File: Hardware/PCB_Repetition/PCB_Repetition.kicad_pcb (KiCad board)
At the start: 2 copper layers, 519.9 x 88.9 mm, 100 parts, among them J1 Conn_01x03, J10 XLR3, J11 XLR3, J12 XLR3, J13 XLR3, J14 XLR3, J15 XLR3, J16 XLR3, J17 XLR3, J18 XLR3, J2 XLR3, J3 XLR3, J4 Conn_01x03, J5 Conn_01x03, J6 Conn_01x03, J7 XLR3, J8 XLR3, J9 XLR3, Q1 SQ2310ES-T1_BE3, Q2 SQ2310ES-T1_BE3, Q3 SQ2310ES-T1_BE3, Q4 SQ2310ES-T1_BE3, Q5 SQ2310ES-T1_BE3, Q6 SQ2310ES-T1_BE3, SW1 SW_SPST, SW2 SW_SPST, SW3 SW_DIP_x02, SW4 SW_DIP_x02, SW5 SW_DIP_x02, SW6 SW_DIP_x02, SW7 SW_DIP_x02, SW8 SW_DIP_x02, U2 ZXBM5210-SP, U4 PCF8575DBR

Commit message: Final change
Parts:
- added G***: LOGO, img:Dessin_CoventGarden, B.Cu at (508.1, 203.5)
- added G***: LOGO, img:Logo_Covent, B.Cu at (508.0, 189.3)
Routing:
- net /INA3_2: track 76.8 -> 77.5 mm
- net GND: vias 878 -> 889
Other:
- board text added: "By Capodagli Janus"

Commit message: finalisation v2 PCB repetition
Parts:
- removed C13, C14, C15, C16, C18: 100n, Capacitor_SMD:C_0603_1608Metric_Pad1.08x0.95mm_HandSolder
- removed D10, D11, D12, D6, D8: WS2812B, LED_SMD:LED_WS2812B_PLCC4_5.0x5.0mm_P3.2mm
- added SW9: SW_DIP_x02, DIP_Switch:DIP_SW_1x02_P2.54mm, F.Cu at (204.7, 185.4)
- C17, C4, C5, Q1, Q2, Q3, Q4, Q5, Q6, R10, R11, R12, R13, R14, R15, R16, R17, R18, R7, R8, R9, U2, U4: moved to F.Cu
- J10, J11, J12, J13, J14, J15, J16, J17, J18, J2, J3, J7, J8, J9: moved to B.Cu
- U1: footprint ESP32_SuperMini:SuperMini SMT -> ESP32_SuperMini:C3_SuperMini
- moved G*** 426.1 mm to (83.7, 165.5)
- moved G*** 424.7 mm to (83.5, 176.9)
- moved J18 270.4 mm to (251.4, 216.0), turned to 180 degrees
- moved C12 250.6 mm to (73.4, 193.8), turned to 90 degrees
- moved J16 200.8 mm to (281.4, 216.0), turned to 180 degrees
- moved J12 186.5 mm to (341.4, 216.0), turned to 180 degrees
- moved U13 179.4 mm to (229.0, 187.0), turned to 0 degrees
- moved SW8 161.5 mm to (246.0, 189.0), turned to -90 degrees
- moved J17 145.5 mm to (244.0, 168.0), turned to 180 degrees
- moved J14 131.6 mm to (311.4, 216.0), turned to 180 degrees
- moved H7 130.0 mm to (417.6, 231.3)
- moved H5 130.0 mm to (417.6, 154.5)
- moved J10 122.4 mm to (371.4, 216.0), turned to 180 degrees
- moved J7 117.5 mm to (394.0, 168.0), turned to 180 degrees
- moved SW3 99.9 mm to (396.0, 189.0), turned to -90 degrees
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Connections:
- net /Relais_XLR1/GND2 renamed /Relais_XLR1/GND_entree
- net /Relais_XLR2/GND2 renamed /Relais_XLR2/GND_entree
- net /Relais_XLR3/GND2 renamed /Relais_XLR3/GND_entree
- net /Relais_XLR4/GND2 renamed /Relais_XLR4/GND_entree
- net /Relais_XLR5/GND2 renamed /Relais_XLR5/GND_entree
- net /Relais_XLR6/GND2 renamed /Relais_XLR6/GND_entree
- D5 pad 2: Net-(D5-DOUT) -> unconnected-(D5-DOUT-Pad2)
- H2 pad 1: unconnected-(H2-Pad1)_2 -> Earth
- H3 pad 1: Earth -> GND
- J10 pad 1: GND -> /Relais_XLR2/GND_sortie
- J12 pad 1: GND -> /Relais_XLR3/GND_sortie
- J14 pad 1: GND -> /Relais_XLR4/GND_sortie
- J16 pad 1: GND -> /Relais_XLR5/GND_sortie
- J18 pad 1: GND -> /Relais_XLR6/GND_sortie
- J8 pad 1: GND -> /Relais_XLR1/GND_sortie
- SW3 pad 1: /GNDA -> GND
- SW3 pad 4: GND -> /Relais_XLR1/GND_sortie
- SW4 pad 1: /GNDA -> GND
- SW4 pad 4: GND -> /Relais_XLR2/GND_sortie
- SW5 pad 1: /GNDA -> GND
- SW5 pad 4: GND -> /Relais_XLR3/GND_sortie
- SW6 pad 1: /GNDB -> GND
- SW6 pad 4: GND -> /Relais_XLR4/GND_sortie
- SW7 pad 1: /GNDB -> GND
- SW7 pad 4: GND -> /Relais_XLR5/GND_sortie
- SW8 pad 1: /GNDB -> GND
- SW8 pad 4: GND -> /Relais_XLR6/GND_sortie
- U1 pad 10: /FWD -> /REV
- U1 pad 11: /REV -> /FWD
- U4 pad 17: unconnected-(U4-P14-Pad17) -> /INA1_1
- U4 pad 18: unconnected-(U4-P15-Pad18) -> /INA1_2
- U4 pad 19: /INA3_2 -> /INA2_1
- U4 pad 20: /INA3_1 -> /INA2_2
- U4 pad 6: /INA2_2 -> /INA3_1
- U4 pad 7: /INA2_1 -> /INA3_2
- U4 pad 8: /INA1_2 -> unconnected-(U4-P4-Pad8)
- U4 pad 9: /INA1_1 -> unconnected-(U4-P5-Pad9)
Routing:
- net /Co_SET: track 459.5 -> 227.5 mm, vias 8 -> 6
- net /Co_ReSET: track 449.3 -> 229.5 mm, vias 8 -> 6
- net /GNDA: track 199.8 -> 24.7 mm, vias 1 -> 0
- net /Relais_XLR4/OUT+: track 196.6 -> 32.9 mm, vias 2 -> 1
- net /GNDB: track 198.4 -> 36.1 mm, vias 4 -> 0
- net /Relais_XLR5/OUT+: track 173.9 -> 33.0 mm, vias 2 -> 1
- net /Relais_XLR4/OUT-: track 176.2 -> 38.5 mm, vias 2 -> 1
- net /Relais_XLR1/OUT-: track 175.8 -> 38.5 mm, vias 2 -> 1
- net /Relais_XLR2/OUT+: track 170.0 -> 32.8 mm, vias 2 -> 1
- net /Relais_XLR1/OUT+: track 167.8 -> 32.8 mm, vias 2 -> 1
- net /Relais_XLR3/OUT-: track 168.7 -> 38.4 mm, vias 2 -> 1
- net /Relais_XLR3/OUT+: track 159.6 -> 32.8 mm, vias 2 -> 1
- net /Relais_XLR6/OUT+: track 153.9 -> 33.0 mm, vias 2 -> 1
- net +5V: track 141.3 -> 23.7 mm, vias 15 -> 22
- net /Relais_XLR5/OUT-: track 155.1 -> 38.4 mm, vias 2 -> 1
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- added copper zone on In2.Cu, net +5V
- added copper zone on B.Cu, net /Phase
- added copper zone on B.Cu, net /Relais1/LINE_Sw
- added copper zone on B.Cu, net /Relais2/LINE_Sw
- added copper zone on B.Cu, net /Relais3/LINE_Sw
- added copper zone on In2.Cu, net Earth
- added copper zone on In1.Cu, net GND
- added copper zone on In2.Cu, net GND
- added copper zone on B.Cu, net LINE
- removed copper zone on B.Cu, net +5V
- removed copper zone on F.Cu, net /Phase
- removed copper zone on F.Cu, net /Relais1/LINE_Sw
- removed copper zone on F.Cu, net /Relais2/LINE_Sw
- removed copper zone on F.Cu, net /Relais3/LINE_Sw
- removed copper zone on F.Cu, net Earth
- removed copper zone on F.Cu, net LINE
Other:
- board size 519.9 x 88.9 mm -> 389.9 x 88.9 mm
- copper layers 2 -> 4

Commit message: ajout vias PCB repetition
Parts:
- moved H4 35.1 mm to (252.0, 191.0)
- moved SW9 3.67 mm to (204.0, 189.0)
- moved H3 1.91 mm to (133.0, 191.0)
- moved H6 1.40 mm to (374.0, 191.0)
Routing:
- net /GNDA: track 24.7 -> 28.6 mm
- net /Co_SET: track 227.5 -> 231.1 mm
- net /GNDB: track 36.1 -> 39.4 mm
- net /Co_ReSET: track 229.5 -> 227.8 mm
- net /A+: track 197.2 -> 198.5 mm
- net /B+: track 138.7 -> 139.8 mm
- net /A-: track 208.2 -> 207.3 mm
- net GND: vias 0 -> 775
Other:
- board text added: "A/B Gnd"

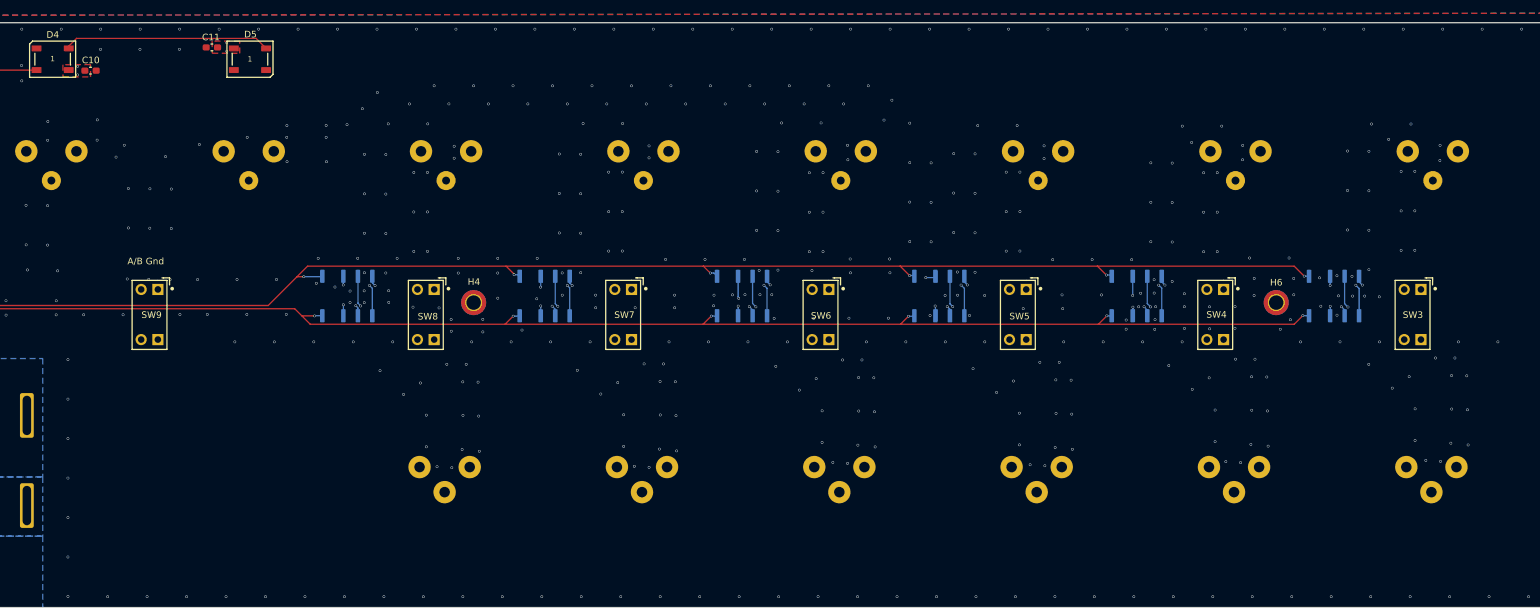
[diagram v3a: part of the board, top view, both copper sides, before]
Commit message: modif Silkscreens PCB repetition et ajout répertoire GERBER
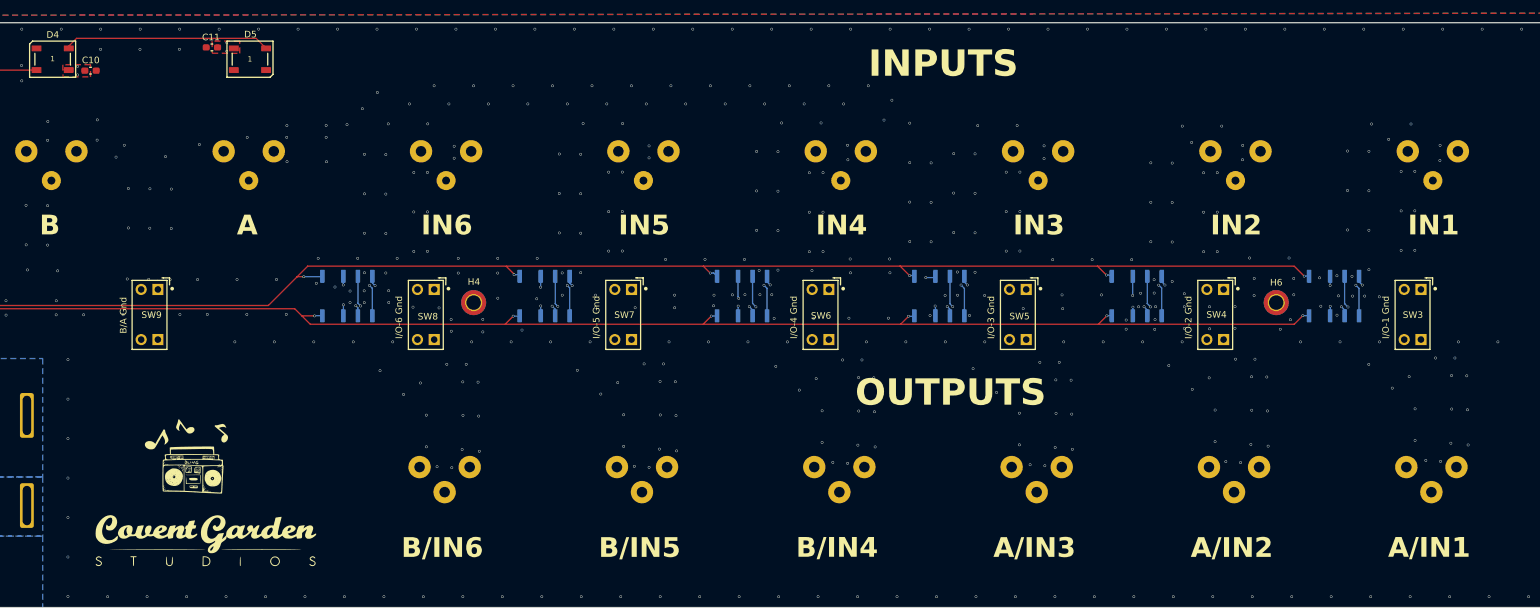
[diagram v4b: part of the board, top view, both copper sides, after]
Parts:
- added G***: LOGO, img:Dessin_CoventGarden, F.Cu at (208.8, 214.7)
- added G***: LOGO, img:Logo_Covent, F.Cu at (211.4, 227.6)
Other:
- board text added: "A"
- board text added: "A/IN1"
- board text added: "A/IN2"
- board text added: "A/IN3"
- board text added: "B"
- board text added: "B/A Gnd"
- board text added: "B/IN4"
- board text added: "B/IN5"
- board text added: "B/IN6"
- board text added: "I/O-1 Gnd"
- board text added: "I/O-2 Gnd"
- board text added: "I/O-3 Gnd"
- board text added: "I/O-4 Gnd"
- board text added: "I/O-5 Gnd"
- board text added: "I/O-6 Gnd"
- board text added: "IN1"
- board text added: "IN2"
- board text added: "IN3"
- board text added: "IN4"
- board text added: "IN5"
- board text added: "IN6"
- board text added: "INPUTS"
- board text added: "OUTPUTS"
- board text removed: "A/B Gnd"

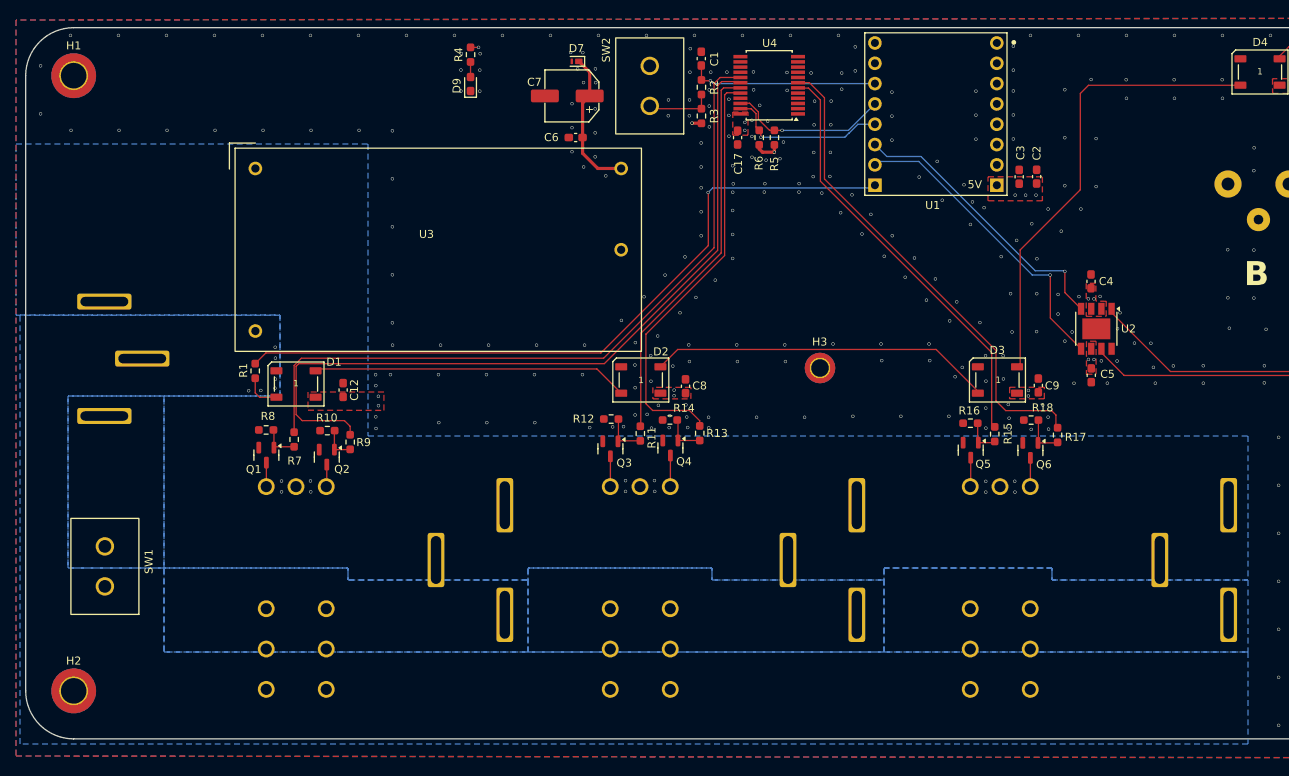
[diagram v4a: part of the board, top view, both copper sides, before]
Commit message: ajout des pinheaders en plus
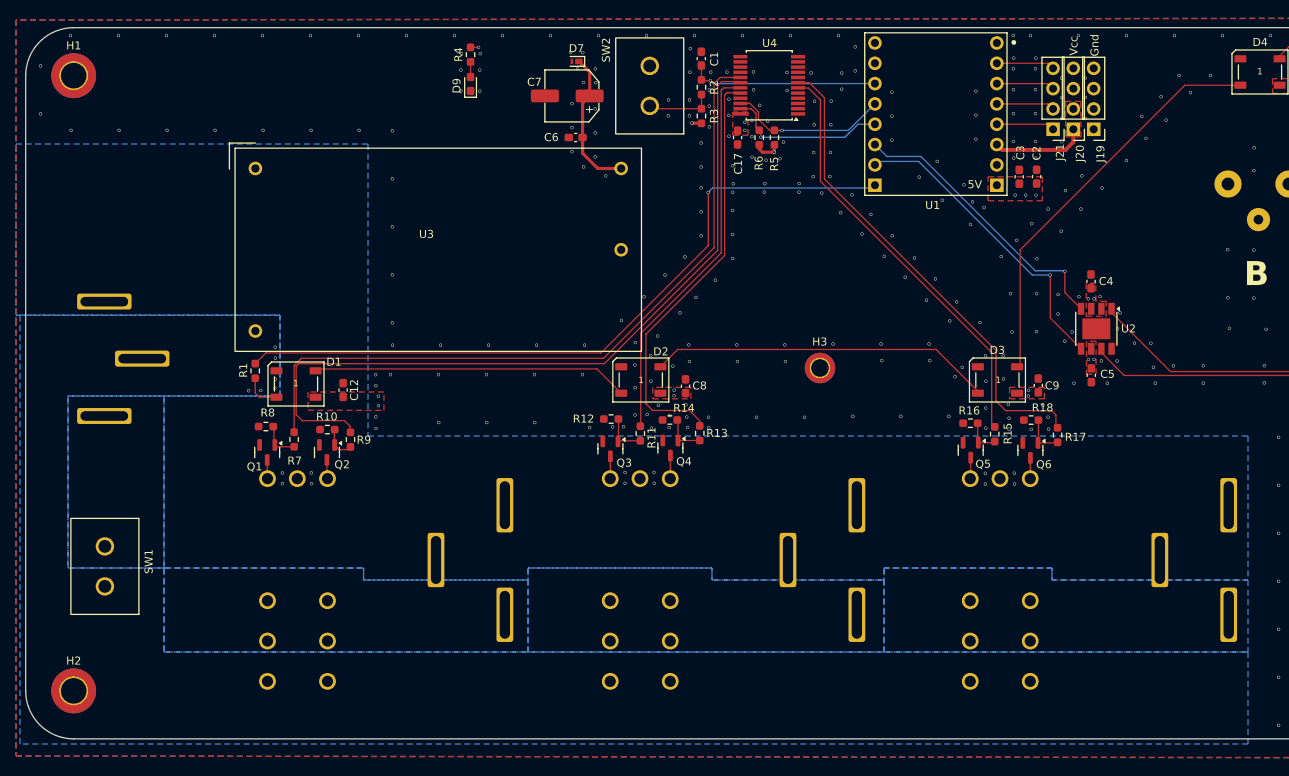
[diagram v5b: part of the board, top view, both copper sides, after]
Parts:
- added J19: Conn_01x04, Connector_PinHeader_2.54mm:PinHeader_1x04_P2.54mm_Vertical, F.Cu at (167.2, 161.2)
- added J20: Conn_01x04, Connector_PinHeader_2.54mm:PinHeader_1x04_P2.54mm_Vertical, F.Cu at (164.7, 161.2)
- added J21: Conn_01x04, Connector_PinHeader_2.54mm:PinHeader_1x04_P2.54mm_Vertical, F.Cu at (162.1, 161.2)
- moved U5 1.01 mm to (67.7, 217.5)
- moved U6 1.00 mm to (110.5, 217.5)
- moved U7 1.00 mm to (155.5, 217.5)
- moved Q2 0.58 mm to (71.4, 201.6)
- moved R8 0.42 mm to (63.7, 198.3)
- moved Q1 0.35 mm to (63.9, 201.6)
- moved R9 0.31 mm to (74.3, 199.9)
- moved R10 0.13 mm to (71.4, 198.7)
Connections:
- U1 pad 2: unconnected-(U1-GPIO1-Pad2) -> /GPIO1
- U1 pad 3: unconnected-(U1-GPIO2-Pad3) -> /GPIO2
- U1 pad 4: unconnected-(U1-GPIO3-Pad4) -> /GPIO3
- U1 pad 5: unconnected-(U1-GPIO4-Pad5) -> /GPIO4
- U1 pad 6: unconnected-(U1-3.3V-Pad6) -> +3.3V
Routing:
- net +3.3V: track 0.00 -> 11.8 mm
- net /GPIO2: track 0.00 -> 7.29 mm
- net /GPIO4: track 0.00 -> 7.29 mm
- net /GPIO3: track 0.00 -> 7.29 mm
- net /GPIO1: track 0.00 -> 7.29 mm
- net Net-(D3-DOUT): track 57.9 -> 50.8 mm
- net Net-(Q6-D): track 3.60 -> 2.60 mm
- net Net-(Q5-D): track 3.64 -> 2.64 mm
- net Net-(Q1-D): track 3.01 -> 2.35 mm
- net GND: vias 775 -> 789
- added copper zone on F.Cu, net +3.3V
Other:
- board text added: "3.3V"
- board text added: "5V"
- board text added: "Gnd"
- board text added: "Vcc"
